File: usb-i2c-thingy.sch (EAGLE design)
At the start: 26 parts, among them IC1 ATTINY85, J1 10103592-0001LF, Q1 220mA/50V/3.5Ω, Q2 220mA/50V/3.5Ω, U1 CJT1117-3.3-SOT223, X1 STEREOJACK

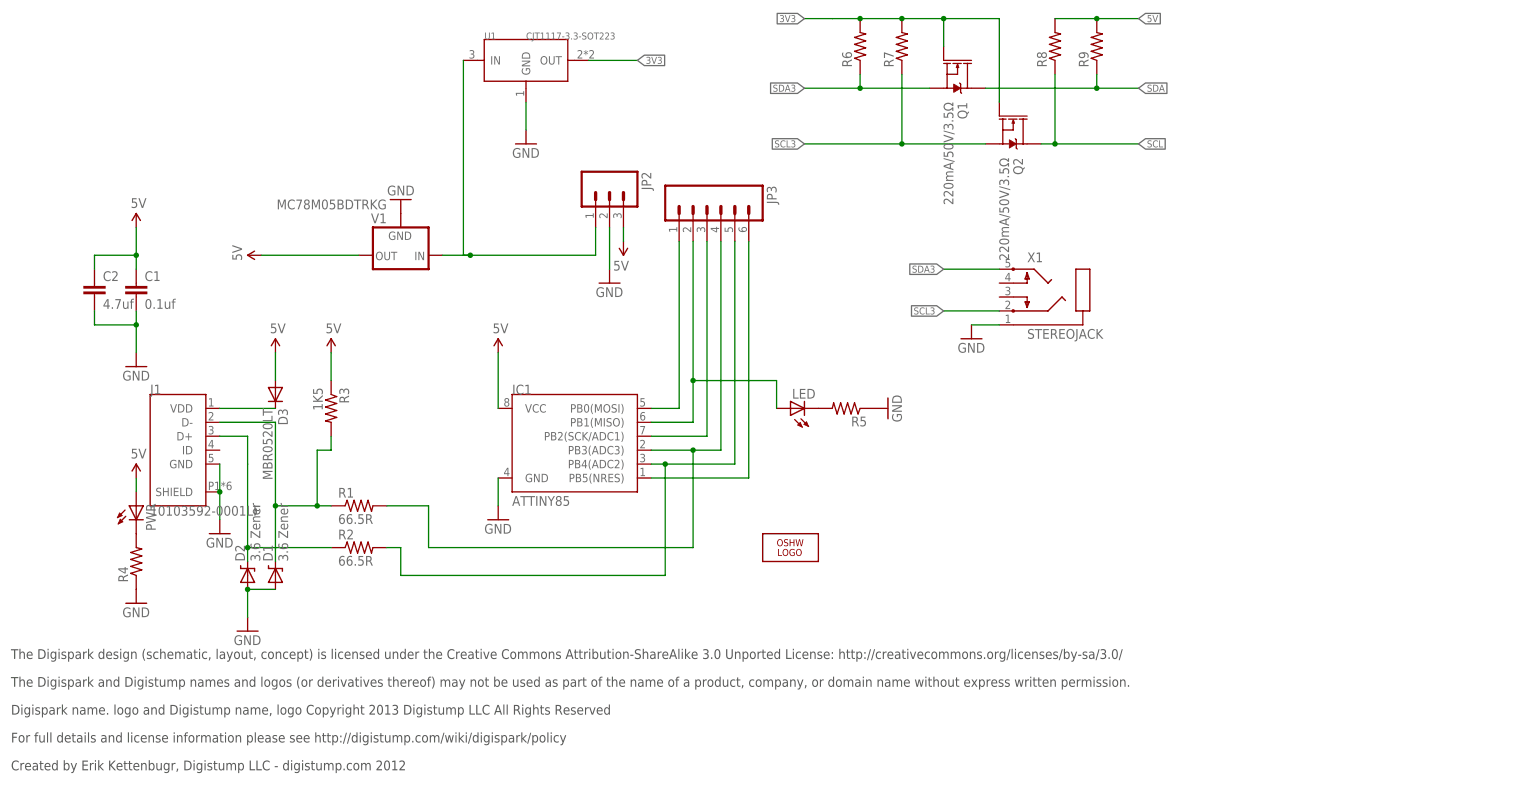
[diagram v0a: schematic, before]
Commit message: Change dimensions, add 603 parts, add SDA/SCL hookup on schematic, jiggle around layout.
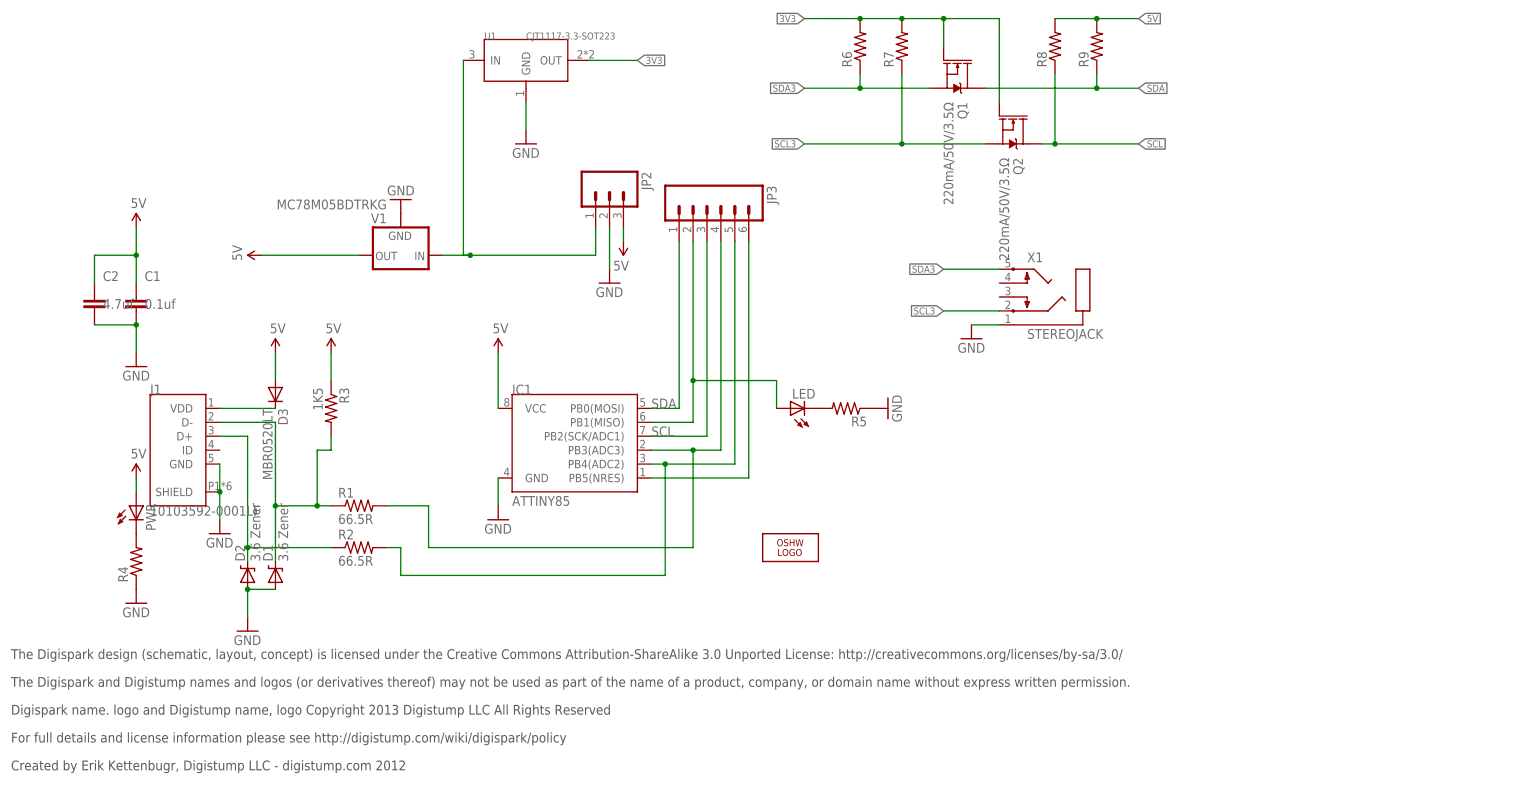
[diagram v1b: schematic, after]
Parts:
- C1: device SparkFun:CAP0402-CAP -> rcl:C-EUC0603
- C2: device SparkFun:CAP0805 -> rcl:C-EUC0603
- R1, R2, R3, R4, R5, R6, R7, R8, R9: device SparkFun:RESISTOR0402-RES -> adafruit:R-US_R0603
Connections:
- removed net N$3: IC1.PB0(MOSI), JP3.1
- removed net N$5: IC1.PB2(SCK/ADC1), JP3.3
- net SCL: now also IC1.PB2(SCK/ADC1), JP3.3
- net SDA: now also IC1.PB0(MOSI), JP3.1
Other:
- moved on the sheet: C1, C2
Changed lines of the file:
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@@
 <part name="D2" library="SparkFun" deviceset="DIODE-ZENER" device="-BZT52" value="3.6 Zener"/>
 <part name="D1" library="SparkFun" deviceset="DIODE-ZENER" device="-BZT52" value="3.6 Zener"/>
-<part name="C1" library="SparkFun" deviceset="CAP" device="0402-CAP" value="0.1uf"/>
-<part name="R1" library="SparkFun" deviceset="RESISTOR" device="0402-RES" value="66.5R"/>
-<part name="R2" library="SparkFun" deviceset="RESISTOR" device="0402-RES" value="66.5R"/>
-<part name="R3" library="SparkFun" deviceset="RESISTOR" device="0402-RES" value="1K5"/>
+<part name="C1" library="rcl" library_urn="urn:adsk.eagle:library:334" deviceset="C-EU" device="C0603" package3d_urn="urn:adsk.eagle:package:23616/2" value="0.1uf"/>
+<part name="R1" library="adafruit" library_urn="urn:adsk.eagle:library:420" deviceset="R-US_" device="R0603" package3d_urn="urn:adsk.eagle:package:6240565/1" value="66.5R"/>
+<part name="R2" library="adafruit" library_urn="urn:adsk.eagle:library:420" deviceset="R-US_" device="R0603" package3d_urn="urn:adsk.eagle:package:6240565/1" value="66.5R"/>
+<part name="R3" library="adafruit" library_urn="urn:adsk.eagle:library:420" deviceset="R-US_" device="R0603" package3d_urn="urn:adsk.eagle:package:6240565/1" value="1K5"/>
 <part name="GND1" library="SparkFun" deviceset="GND" device=""/>
 <part name="U$1" library="SparkFun" deviceset="5V" device=""/>
@@
 <part name="GND3" library="SparkFun" deviceset="GND" device=""/>
 <part name="LED" library="SparkFun" deviceset="LED" device="0603"/>
-<part name="R5" library="SparkFun" deviceset="RESISTOR" device="0402-RES"/>
+<part name="R5" library="adafruit" library_urn="urn:adsk.eagle:library:420" deviceset="R-US_" device="R0603" package3d_urn="urn:adsk.eagle:package:6240565/1"/>
 <part name="GND6" library="SparkFun" deviceset="GND" device=""/>
 <part name="GND10" library="SparkFun" deviceset="GND" device=""/>
@@
 <part name="D3" library="diode" deviceset="MBR0520LT" device=""/>
 <part name="PWR" library="SparkFun" deviceset="LED" device="0603"/>
-<part name="R4" library="SparkFun" deviceset="RESISTOR" device="0402-RES"/>
+<part name="R4" library="adafruit" library_urn="urn:adsk.eagle:library:420" deviceset="R-US_" device="R0603" package3d_urn="urn:adsk.eagle:package:6240565/1"/>
 <part name="GND12" library="SparkFun" deviceset="GND" device=""/>
 <part name="U$7" library="SparkFun" deviceset="5V" device=""/>
 <part name="U$5" library="SparkFun" deviceset="5V" device=""/>
 <part name="GND13" library="SparkFun" deviceset="GND" device=""/>
-<part name="C2" library="SparkFun" deviceset="CAP" device="0805" value="4.7uf"/>
+<part name="C2" library="rcl" library_urn="urn:adsk.eagle:library:334" deviceset="C-EU" device="C0603" package3d_urn="urn:adsk.eagle:package:23616/2" value="4.7uf"/>
 <part name="JP2" library="SparkFun" deviceset="M03" device="PTH"/>
 <part name="JP3" library="SparkFun" deviceset="M06" device="SIP"/>
@@
 <part name="Q1" library="SparkFun-DiscreteSemi" library_urn="urn:adsk.eagle:library:514" deviceset="MOSFET-NCH" device="-BSS138" package3d_urn="urn:adsk.eagle:package:38446/1" value="220mA/50V/3.5Ω"/>
 <part name="Q2" library="SparkFun-DiscreteSemi" library_urn="urn:adsk.eagle:library:514" deviceset="MOSFET-NCH" device="-BSS138" package3d_urn="urn:adsk.eagle:package:38446/1" value="220mA/50V/3.5Ω"/>
-<part name="R6" library="SparkFun" deviceset="RESISTOR" device="0402-RES"/>
-<part name="R7" library="SparkFun" deviceset="RESISTOR" device="0402-RES"/>
-<part name="R8" library="SparkFun" deviceset="RESISTOR" device="0402-RES"/>
-<part name="R9" library="SparkFun" deviceset="RESISTOR" device="0402-RES"/>
+<part name="R6" library="adafruit" library_urn="urn:adsk.eagle:library:420" deviceset="R-US_" device="R0603" package3d_urn="urn:adsk.eagle:package:6240565/1"/>
+<part name="R7" library="adafruit" library_urn="urn:adsk.eagle:library:420" deviceset="R-US_" device="R0603" package3d_urn="urn:adsk.eagle:package:6240565/1"/>
+<part name="R8" library="adafruit" library_urn="urn:adsk.eagle:library:420" deviceset="R-US_" device="R0603" package3d_urn="urn:adsk.eagle:package:6240565/1"/>
+<part name="R9" library="adafruit" library_urn="urn:adsk.eagle:library:420" deviceset="R-US_" device="R0603" package3d_urn="urn:adsk.eagle:package:6240565/1"/>
 <part name="U1" library="Seeed-IC" library_urn="urn:adsk.eagle:library:470" deviceset="PMIC-CJT1117-3.3(SOT223)" device="" package3d_urn="urn:adsk.eagle:package:32638/1" value="CJT1117-3.3-SOT223"/>
 <part name="GND5" library="SparkFun" deviceset="GND" device=""/>
@@
 <pinref part="C1" gate="G$1" pin="2"/>
 <pinref part="GND13" gate="1" pin="GND"/>
-<wire x1="-20.32" y1="63.5" x2="-20.32" y2="60.96" width="0.1524" layer="91"/>
 <wire x1="-20.32" y1="60.96" x2="-20.32" y2="55.88" width="0.1524" layer="91"/>
 <wire x1="-20.32" y1="60.96" x2="-27.94" y2="60.96" width="0.1524" layer="91"/>
 <pinref part="C2" gate="G$1" pin="2"/>
-<wire x1="-27.94" y1="60.96" x2="-27.94" y2="63.5" width="0.1524" layer="91"/>
 <junction x="-20.32" y="60.96"/>
 </segment>
@@
 <wire x1="-20.32" y1="78.74" x2="-20.32" y2="73.66" width="0.1524" layer="91"/>
 <pinref part="C2" gate="G$1" pin="1"/>
-<wire x1="-20.32" y1="73.66" x2="-20.32" y2="71.12" width="0.1524" layer="91"/>
-<wire x1="-27.94" y1="71.12" x2="-27.94" y2="73.66" width="0.1524" layer="91"/>
+<wire x1="-20.32" y1="73.66" x2="-20.32" y2="68.58" width="0.1524" layer="91"/>
+<wire x1="-27.94" y1="68.58" x2="-27.94" y2="73.66" width="0.1524" layer="91"/>
 <wire x1="-27.94" y1="73.66" x2="-20.32" y2="73.66" width="0.1524" layer="91"/>
 <junction x="-20.32" y="73.66"/>
@@
 <wire x1="86.36" y1="38.1" x2="86.36" y2="76.2" width="0.1524" layer="91"/>
 <junction x="81.28" y="38.1"/>
-</segment>
-</net>
-<net name="N$3" class="0">
-<segment>
-<pinref part="IC1" gate="G$1" pin="PB0(MOSI)"/>
-<wire x1="73.66" y1="45.72" x2="78.74" y2="45.72" width="0.1524" layer="91"/>
-<pinref part="JP3" gate="G$1" pin="1"/>
-<wire x1="78.74" y1="45.72" x2="78.74" y2="76.2" width="0.1524" layer="91"/>
-</segment>
-</net>
-<net name="N$5" class="0">
-<segment>
-<pinref part="IC1" gate="G$1" pin="PB2(SCK/ADC1)"/>
-<wire x1="73.66" y1="40.64" x2="83.82" y2="40.64" width="0.1524" layer="91"/>
-<wire x1="83.82" y1="40.64" x2="83.82" y2="76.2" width="0.1524" layer="91"/>
-<pinref part="JP3" gate="G$1" pin="3"/>
 </segment>
 </net>
@@
 <label x="162.56" y="104.14" size="1.27" layer="95" xref="yes"/>
 </segment>
+<segment>
+<pinref part="IC1" gate="G$1" pin="PB0(MOSI)"/>
+<wire x1="73.66" y1="45.72" x2="78.74" y2="45.72" width="0.1524" layer="91"/>
+<pinref part="JP3" gate="G$1" pin="1"/>
+<wire x1="78.74" y1="45.72" x2="78.74" y2="76.2" width="0.1524" layer="91"/>
+<label x="73.66" y="45.72" size="1.778" layer="95"/>
+</segment>
 </net>
 <net name="SCL" class="0">
@@
 <junction x="147.32" y="93.98"/>
 <label x="162.56" y="93.98" size="1.27" layer="95" xref="yes"/>
+</segment>
+<segment>
+<pinref part="IC1" gate="G$1" pin="PB2(SCK/ADC1)"/>
+<wire x1="73.66" y1="40.64" x2="83.82" y2="40.64" width="0.1524" layer="91"/>
+<wire x1="83.82" y1="40.64" x2="83.82" y2="76.2" width="0.1524" layer="91"/>
+<pinref part="JP3" gate="G$1" pin="3"/>
+<label x="73.66" y="40.64" size="1.778" layer="95"/>
 </segment>
 </net>
@@
 packages will not be understood (or retained) with this version.
 </note>
+<note version="8.4" severity="warning">
+Since Version 8.4, EAGLE supports properties for SPICE simulation.
+Probes in schematics and SPICE mapping objects found in parts and library devices
+will not be understood with this version. Update EAGLE to the latest version
+for full support of SPICE simulation.
+</note>
 </compatibility>
